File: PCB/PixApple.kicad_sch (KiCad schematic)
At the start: 38 parts, among them J10 Conn_01x11, J11 Conn_01x11, J28 Conn_01x01_Pin, J29 Conn_01x01_Pin, J3 Conn_01x01_Pin, J30 Conn_01x01_Pin, J4 Conn_01x01_Pin, J5 Conn_01x05_Pin, J6 Conn_01x02_Pin, J7 Conn_01x01_Pin, J8 Conn_02x03_Odd_Even, J9 Conn_01x04_Pin, SW1 SW_Push, SW2 SW_Push, U1 RP2040

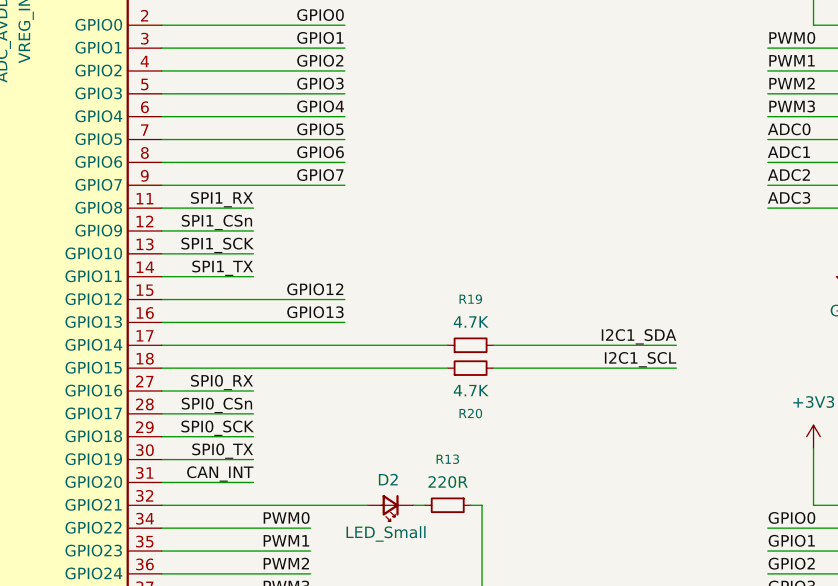
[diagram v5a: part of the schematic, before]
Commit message: Fix pullup, connected 3V3 completely
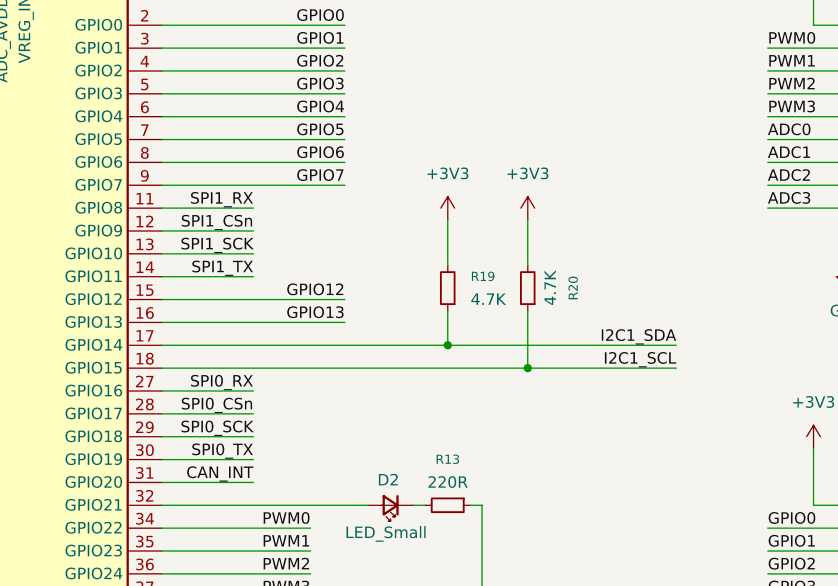
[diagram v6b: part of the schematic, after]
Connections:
- net +3V3: now also R19.2, R20.2
- net I2C1_SCL: now also R20.1, U1.18 (GPIO15); no longer R20.2
- net I2C1_SDA: now also R19.1, U1.17 (GPIO14); no longer R19.2
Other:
- moved on the sheet: R19, R20
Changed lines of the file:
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@@
 	)
 	(junction
+		(at 163.83 100.33)
+		(diameter 0)
+		(color 0 0 0 0)
+	)
+	(junction
 		(at 109.22 21.59)
 		(diameter 0)
@@
 	)
 	(junction
+		(at 172.72 102.87)
+		(diameter 0)
+		(color 0 0 0 0)
+	)
+	(junction
 		(at 114.3 31.75)
 		(diameter 0)
@@
 	(wire
 		(pts
-			(xy 168.91 102.87) (xy 189.23 102.87)
-		)
-		(stroke
-			(width 0)
-			(type default)
-		)
-	)
-	(wire
-		(pts
 			(xy 132.08 128.27) (xy 148.59 128.27)
 		)
@@
 	(wire
 		(pts
+			(xy 172.72 86.36) (xy 172.72 91.44)
+		)
+		(stroke
+			(width 0)
+			(type default)
+		)
+	)
+	(wire
+		(pts
 			(xy 213.36 118.11) (xy 204.47 118.11)
 		)
@@
 	(wire
 		(pts
+			(xy 172.72 96.52) (xy 172.72 102.87)
+		)
+		(stroke
+			(width 0)
+			(type default)
+		)
+	)
+	(wire
+		(pts
 			(xy 109.22 31.75) (xy 109.22 49.53)
 		)
@@
 	(wire
 		(pts
+			(xy 163.83 100.33) (xy 189.23 100.33)
+		)
+		(stroke
+			(width 0)
+			(type default)
+		)
+	)
+	(wire
+		(pts
 			(xy 60.96 110.49) (xy 81.28 110.49)
 		)
@@
 	(wire
 		(pts
+			(xy 163.83 96.52) (xy 163.83 100.33)
+		)
+		(stroke
+			(width 0)
+			(type default)
+		)
+	)
+	(wire
+		(pts
 			(xy 111.76 49.53) (xy 111.76 57.15)
 		)
@@
 	(wire
 		(pts
-			(xy 132.08 102.87) (xy 163.83 102.87)
+			(xy 132.08 102.87) (xy 172.72 102.87)
 		)
 		(stroke
@@
 	(wire
 		(pts
+			(xy 163.83 86.36) (xy 163.83 91.44)
+		)
+		(stroke
+			(width 0)
+			(type default)
+		)
+	)
+	(wire
+		(pts
 			(xy 132.08 105.41) (xy 142.24 105.41)
 		)
@@
 	(wire
 		(pts
-			(xy 168.91 100.33) (xy 189.23 100.33)
-		)
-		(stroke
-			(width 0)
-			(type default)
-		)
-	)
-	(wire
-		(pts
 			(xy 90.17 182.88) (xy 95.25 182.88)
 		)
@@
 	(wire
 		(pts
+			(xy 172.72 102.87) (xy 189.23 102.87)
+		)
+		(stroke
+			(width 0)
+			(type default)
+		)
+	)
+	(wire
+		(pts
 			(xy 213.36 120.65) (xy 199.39 120.65)
 		)
@@
 	(symbol
 		(lib_id "Device:R_Small")
-		(at 166.37 102.87 90)
+		(at 172.72 93.98 180)
 		(unit 1)
 		(exclude_from_sim no)
@@
 		(dnp no)
 		(property "Reference" "R20"
-			(at 166.37 107.95 90)
+			(at 177.8 93.98 90)
 			(effects
 				(font
@@
 		)
 		(property "Value" "4.7K"
-			(at 166.37 105.41 90)
+			(at 175.26 93.98 90)
 			(effects
 				(font
@@
 		)
 		(property "Footprint" "Resistor_SMD:R_0603_1608Metric_Pad0.98x0.95mm_HandSolder"
-			(at 166.37 102.87 0)
+			(at 172.72 93.98 0)
 			(effects
 				(font
@@
 		)
 		(property "Datasheet" "~"
-			(at 166.37 102.87 0)
+			(at 172.72 93.98 0)
 			(effects
 				(font
@@
 		)
 		(property "Description" "Resistor, small symbol"
-			(at 166.37 102.87 0)
+			(at 172.72 93.98 0)
 			(effects
 				(font
@@
 	)
 	(symbol
+		(lib_id "power:+3V3")
+		(at 163.83 86.36 0)
+		(unit 1)
+		(exclude_from_sim no)
+		(in_bom yes)
+		(on_board yes)
+		(dnp no)
+		(fields_autoplaced yes)
+		(property "Reference" "#PWR054"
+			(at 163.83 90.17 0)
+			(effects
+				(font
+					(size 1.27 1.27)
+				)
+				(hide yes)
+			)
+		)
+		(property "Value" "+3V3"
+			(at 163.83 81.28 0)
+			(effects
+				(font
+					(size 1.27 1.27)
+				)
+			)
+		)
+		(property "Footprint" ""
+			(at 163.83 86.36 0)
+			(effects
+				(font
+					(size 1.27 1.27)
+				)
+				(hide yes)
+			)
+		)
+		(property "Datasheet" ""
+			(at 163.83 86.36 0)
+			(effects
+				(font
+					(size 1.27 1.27)
+				)
+				(hide yes)
+			)
+		)
+		(property "Description" "Power symbol creates a global label with name \"+3V3\""
+			(at 163.83 86.36 0)
+			(effects
+				(font
+					(size 1.27 1.27)
+				)
+				(hide yes)
+			)
+		)
+		(pin "1"
+		)
+		(instances
+			(project ""
+				(path "/e83b0aa6-9c26-4054-989c-9d9c9a775b37"
+					(reference "#PWR054")
+					(unit 1)
+				)
+			)
+		)
+	)
+	(symbol
 		(lib_id "Connector:Conn_01x01_Pin")
 		(at 254 13.97 270)
@@
 	(symbol
 		(lib_id "Device:R_Small")
-		(at 166.37 100.33 90)
+		(at 163.83 93.98 180)
 		(unit 1)
 		(exclude_from_sim no)
@@
 		(fields_autoplaced yes)
 		(property "Reference" "R19"
-			(at 166.37 95.25 90)
+			(at 166.37 92.7099 0)
 			(effects
 				(font
 					(size 1.016 1.016)
 				)
+				(justify right)
 			)
 		)
 		(property "Value" "4.7K"
-			(at 166.37 97.79 90)
+			(at 166.37 95.2499 0)
 			(effects
 				(font
 					(size 1.27 1.27)
 				)
+				(justify right)
 			)
 		)
 		(property "Footprint" "Resistor_SMD:R_0603_1608Metric_Pad0.98x0.95mm_HandSolder"
-			(at 166.37 100.33 0)
+			(at 163.83 93.98 0)
 			(effects
 				(font
@@
 		)
 		(property "Datasheet" "~"
-			(at 166.37 100.33 0)
+			(at 163.83 93.98 0)
 			(effects
 				(font
@@
 		)
 		(property "Description" "Resistor, small symbol"
-			(at 166.37 100.33 0)
+			(at 163.83 93.98 0)
 			(effects
 				(font
@@
 					(unit 1)
 				)
+			)
+		)
+	)
+	(symbol
+		(lib_id "power:+3V3")
+		(at 172.72 86.36 0)
+		(unit 1)
+		(exclude_from_sim no)
+		(in_bom yes)
+		(on_board yes)
+		(dnp no)
+		(fields_autoplaced yes)
+		(property "Reference" "#PWR055"
+			(at 172.72 90.17 0)
+			(effects
+				(font
+					(size 1.27 1.27)
+				)
+				(hide yes)
+			)
+		)
+		(property "Value" "+3V3"
+			(at 172.72 81.28 0)
+			(effects
+				(font
+					(size 1.27 1.27)
+				)
+			)
+		)
+		(property "Footprint" ""
+			(at 172.72 86.36 0)
+			(effects
+				(font
+					(size 1.27 1.27)
+				)
+				(hide yes)
+			)
+		)
+		(property "Datasheet" ""
+			(at 172.72 86.36 0)
+			(effects
+				(font
+					(size 1.27 1.27)
+				)
+				(hide yes)
+			)
+		)
+		(property "Description" "Power symbol creates a global label with name \"+3V3\""
+			(at 172.72 86.36 0)
+			(effects
+				(font
+					(size 1.27 1.27)
+				)
+				(hide yes)
+			)
+		)
+		(pin "1"
+		)
+		(instances
+			(project ""
+				(path "/e83b0aa6-9c26-4054-989c-9d9c9a775b37"
+					(reference "#PWR055")
+					(unit 1)
+				)

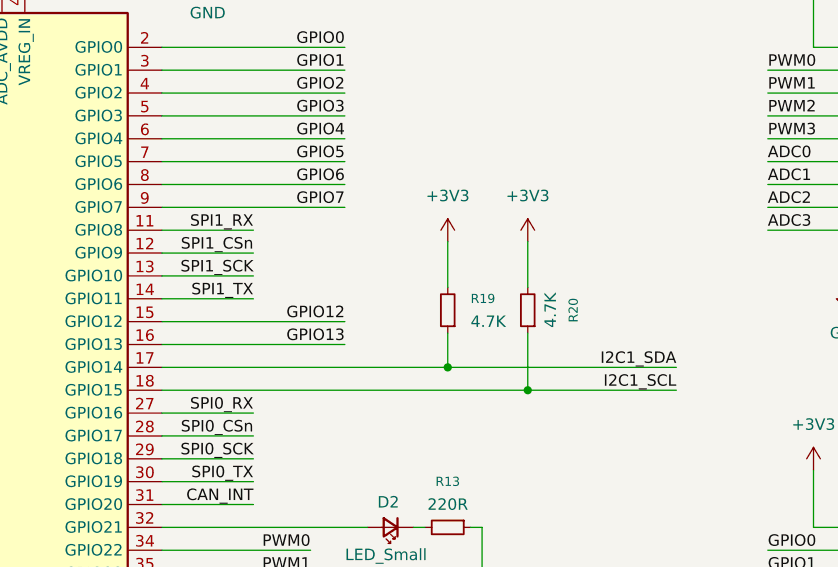
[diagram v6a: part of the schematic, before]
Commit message: esd, pullup, error fix
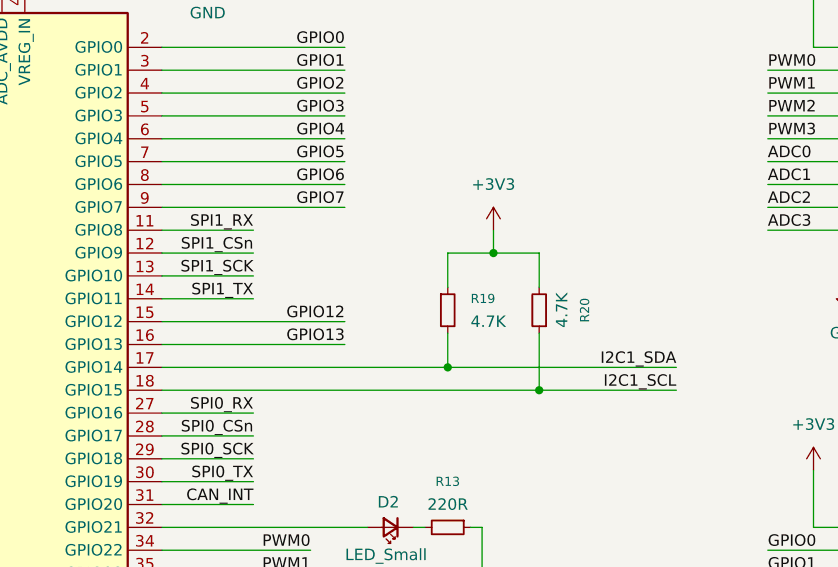
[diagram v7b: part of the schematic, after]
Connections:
- net +3V3: now also R19.1; no longer R19.2
- net I2C1_SDA: now also R19.2; no longer R19.1
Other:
- moved on the sheet: R19, R20
